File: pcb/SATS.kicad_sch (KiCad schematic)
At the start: 3 parts, among them J1 Raspberry_Pi_2_3, U1 MCP23017_SP, U2 MCP23017_SP

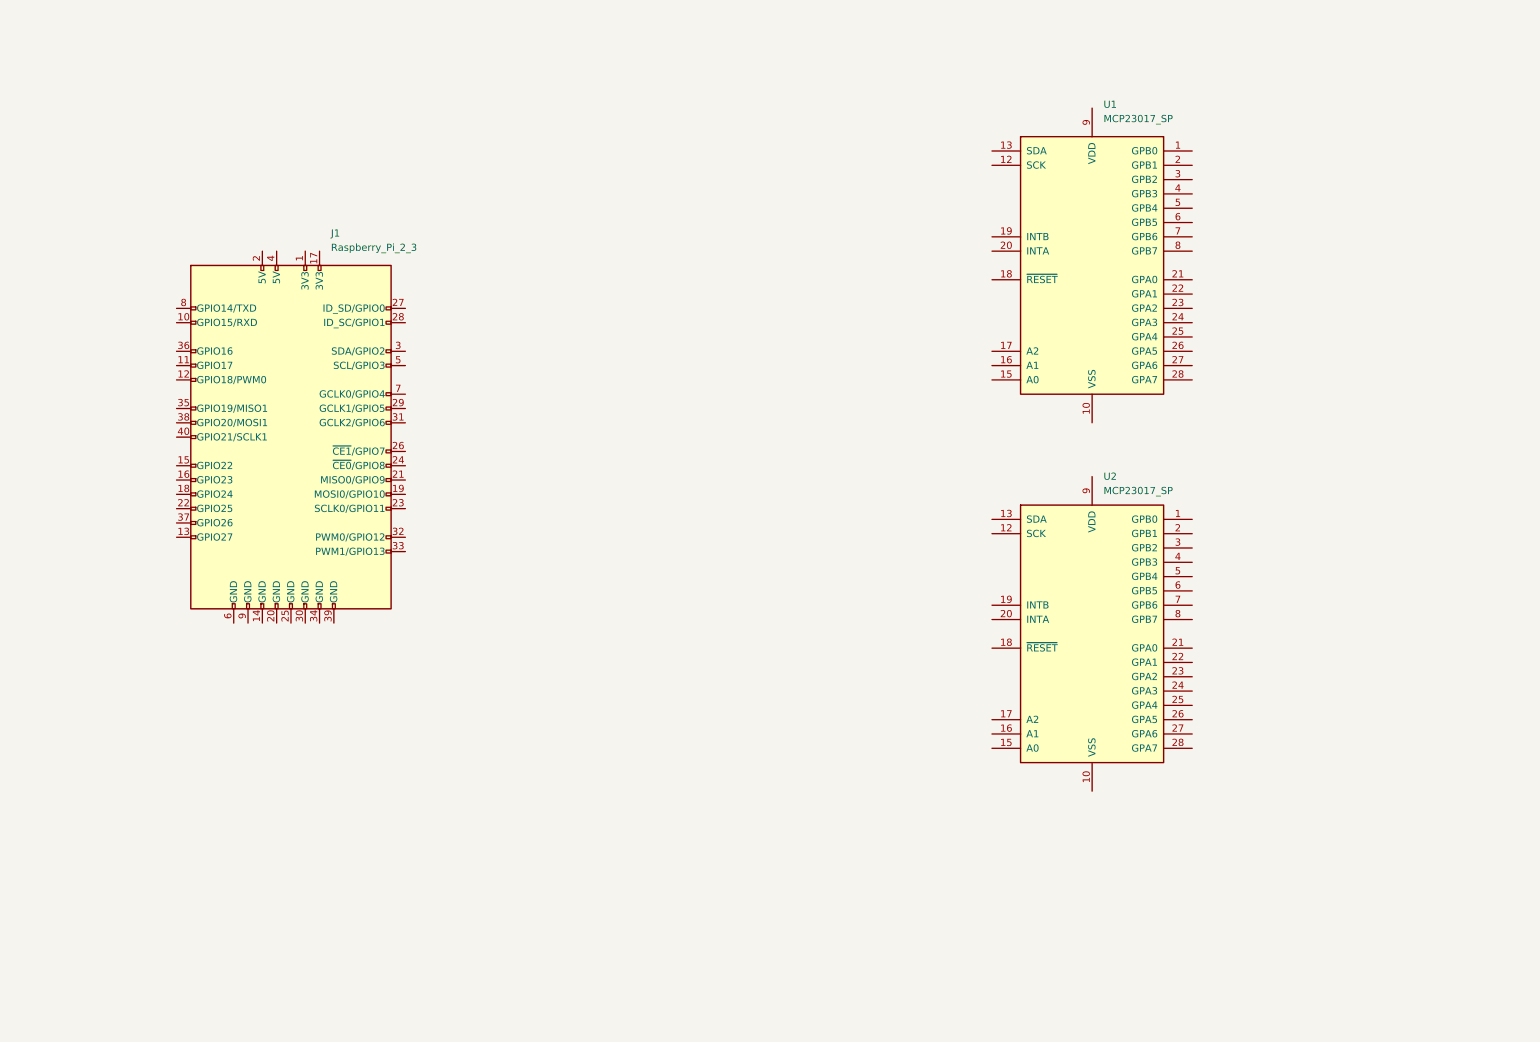
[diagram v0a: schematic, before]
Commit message: Add Solenoid circuit
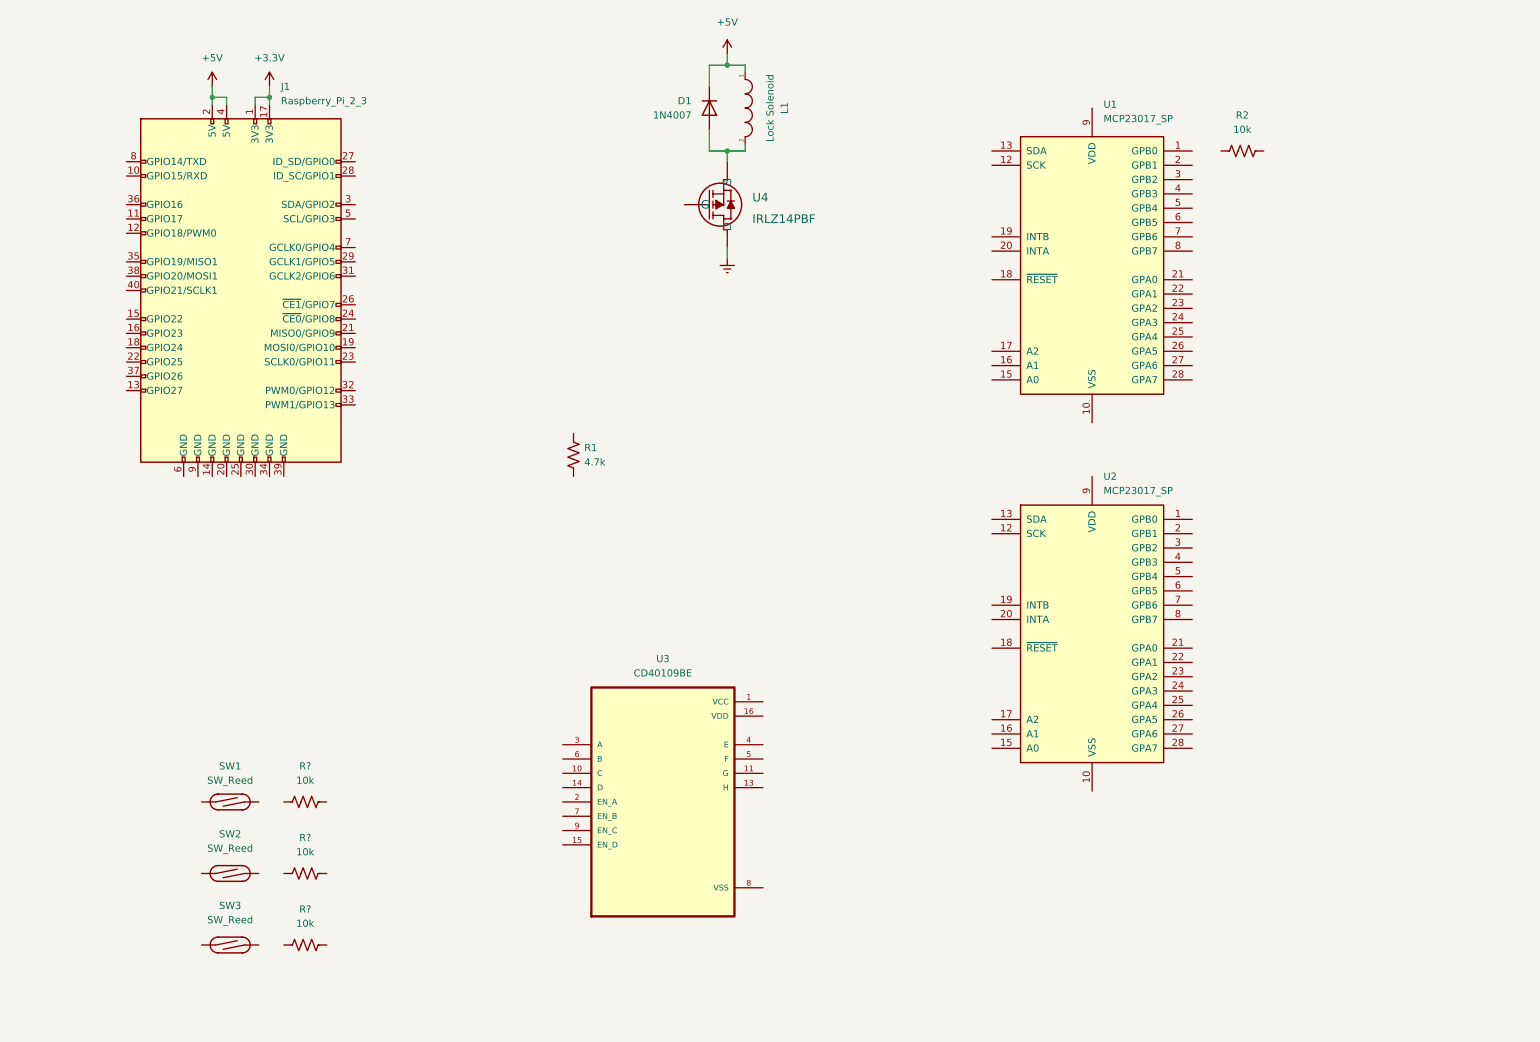
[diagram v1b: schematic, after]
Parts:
- added D1: 1N4007, Diode_THT:D_DO-41_SOD81_P10.16mm_Horizontal, symbol Diode:1N4007
- added L1: Lock Solenoid, symbol pspice:INDUCTOR
- added R1: 4.7k, symbol Device:R_US
- added R2, R? (x3): 10k, symbol Device:R_US
- added SW1, SW2, SW3: SW_Reed, symbol Switch:SW_Reed
- added U3: CD40109BE, DIP794W45P254L1969H508Q16, symbol CD40109BE:CD40109BE
- added U4: IRLZ14PBF, TO220AB_VIS, symbol IRLZ14PBF:IRLZ14PBF
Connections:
- net +3V3: now reaches J1.1 (3V3)
- net +3V3: now also J1.17 (3V3)
- net +5V: now reaches J1.2 (5V)
- net +5V: now also J1.4 (5V), D1.1 (K), L1.1
- new net: D1.2 (A), L1.2, U4.3 (S)
- new net Earth: U4.2 (D)
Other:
- moved on the sheet: J1

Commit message: Start Net building
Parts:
- removed R2: 10k, symbol Device:R_US
- added C1, C2: 100nF, symbol Device:C
- gave numbers to parts that had none: 3
- renumbered R1 to R4
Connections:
- net +3V3: now also R1.2, R2.2, R3.2, R4.2, U1.18 (~{RESET}), U1.9 (VDD), U2.17 (A2), U2.18 (~{RESET}), U2.9 (VDD), C1.1, C2.1
- net Earth: now also J1.14 (GND), J1.20 (GND), J1.25 (GND), J1.30 (GND), J1.34 (GND), J1.39 (GND), J1.6 (GND), J1.9 (GND), SW1.1, SW2.1, SW3.1, U1.10 (VSS), U1.15 (A0), U1.16 (A1), U1.17 (A2), U2.10 (VSS), U2.15 (A0), U2.16 (A1), C1.2, C2.2
- net Third Reed: now reaches R3.1
- net Third Reed: now also J1.28 (ID_SC/GPIO1), SW3.2
- net SCL: now reaches U1.12 (SCK)
- net SCL: now also J1.5 (SCL/GPIO3), U2.12 (SCK)
- net SDA: now reaches U1.13 (SDA)
- net SDA: now also J1.3 (SDA/GPIO2), U2.13 (SDA)
- net Int 1B: now reaches U1.19 (INTB)
- net Int 1B: now also J1.11 (GPIO17), U2.19 (INTB)
- net Int 1A: now reaches U1.20 (INTA)
- net Int 1A: now also J1.7 (GCLK0/GPIO4), U2.20 (INTA)
- net Main Door: now reaches R1.1
- net Main Door: now also J1.24 (~{CE0}/GPIO8), SW1.2
- net Serv Door: now reaches R2.1
- net Serv Door: now also J1.26 (~{CE1}/GPIO7), SW2.2
- net Int 2A: now reaches J1.13 (GPIO27)
- net Int 2B: now reaches J1.15 (GPIO22)
- net LED Sig: now reaches J1.19 (MOSI0/GPIO10)
- net 1-Wire: now reaches J1.21 (MISO0/GPIO9)
- net 1-Wire: now also R4.1
- net Latch: now reaches J1.22 (GPIO25)
- net Latch: now also U4.1 (G)
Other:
- moved on the sheet: D1, J1, L1, R1, R2, R3, R4, SW1, SW2, SW3, U1, U3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

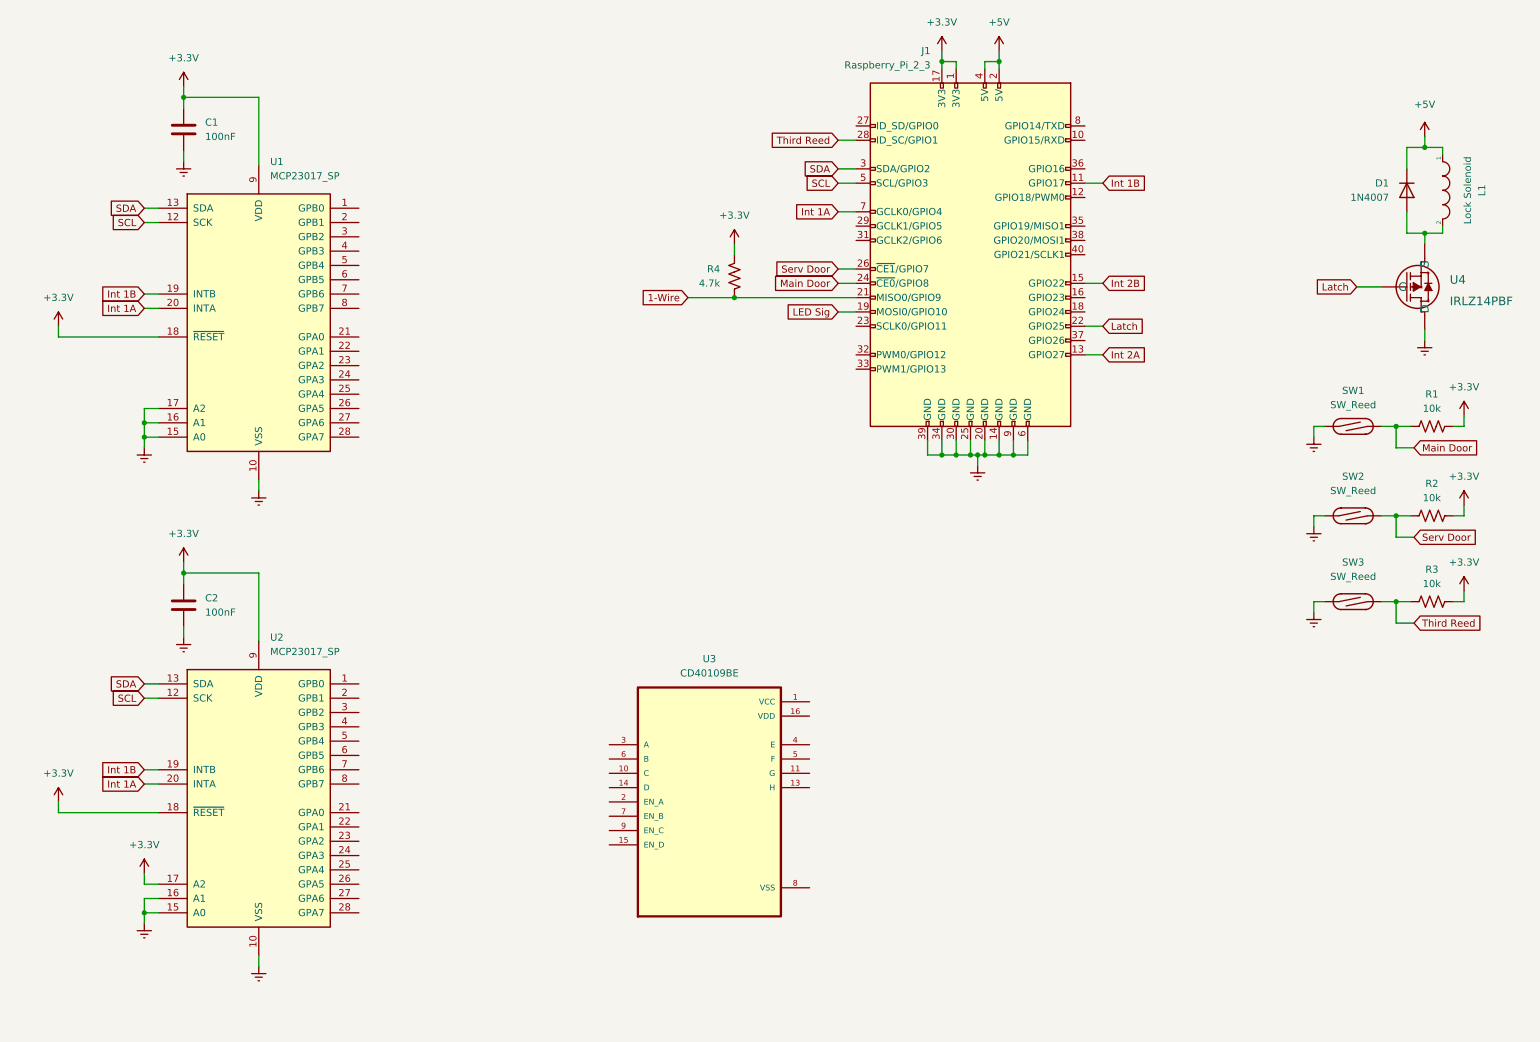
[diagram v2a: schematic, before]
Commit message: remove unneeded pullups, add level shifter ins
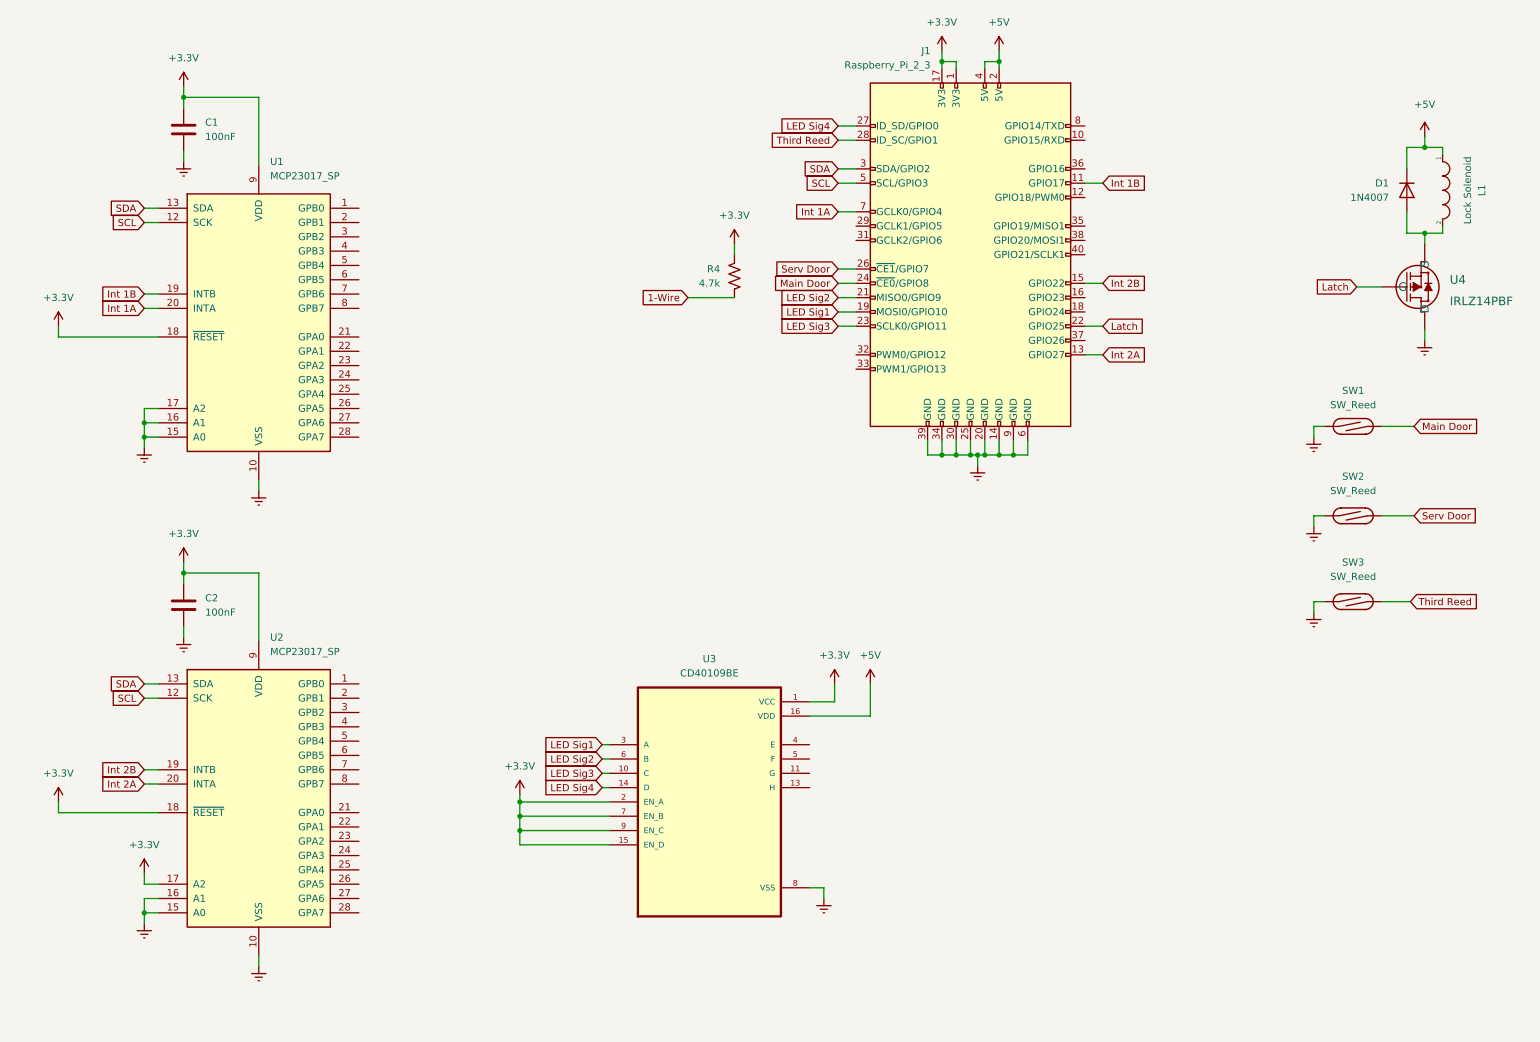
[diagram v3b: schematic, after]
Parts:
- removed R1, R2, R3: 10k, symbol Device:R_US
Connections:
- net LED Sig is gone; now on net LED Sig1: J1.19 (MOSI0/GPIO10)
- net +3V3: now also U3.1 (VCC), U3.15 (EN_D), U3.2 (EN_A), U3.7 (EN_B), U3.9 (EN_C)
- net +5V: now also U3.16 (VDD)
- net 1-Wire: no longer J1.21 (MISO0/GPIO9)
- net Earth: now also U3.8 (VSS)
- net Int 1A: no longer U2.20 (INTA)
- net Int 1B: no longer U2.19 (INTB)
- net Int 2A: now also U2.20 (INTA)
- net Int 2B: now also U2.19 (INTB)
- net LED Sig3: now reaches U3.10 (C)
- net LED Sig3: now also J1.23 (SCLK0/GPIO11)
- net LED Sig4: now reaches U3.14 (D)
- net LED Sig4: now also J1.27 (ID_SD/GPIO0)
- net LED Sig1: now reaches U3.3 (A)
- net LED Sig2: now reaches U3.6 (B)
- net LED Sig2: now also J1.21 (MISO0/GPIO9)
